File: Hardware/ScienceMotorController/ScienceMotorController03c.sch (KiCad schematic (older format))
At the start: 16 parts

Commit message: changed everything to actuation, added schottky diode, added A/B flags to tiva
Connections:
- net +12V renamed +12VA
- net +3V3 renamed +3.3VA
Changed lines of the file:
@@
 	6950 4250 6950 4150
 Connection ~ 6950 4150
-$Comp
-L power:+12V #PWR?
-U 1 1 5FA7B7CE
-P 7150 4000
-AR Path="/5F7D111E/5FA7B7CE" Ref="#PWR?"  Part="1"
-AR Path="/5F7D111E/5FA660A7/5FA7B7CE" Ref="#PWR?"  Part="1"
-F 0 "#PWR?" H 7150 3850 50  0001 C CNN
-F 1 "+12V" H 7165 4173 50  0000 C CNN
-F 2 "" H 7150 4000 50  0001 C CNN
-F 3 "" H 7150 4000 50  0001 C CNN
-	1    7150 4000
-	1    0    0    -1
-$EndComp
 Wire Wire Line
 	7150 4000 7150 4050
@@
 Wire Wire Line
 	4950 4200 4800 4200
-$Comp
-L power:+3.3V #PWR?
-U 1 1 5FA7B80F
-P 4800 4200
-AR Path="/5F7D111E/5FA7B80F" Ref="#PWR?"  Part="1"
-AR Path="/5F7D111E/5FA660A7/5FA7B80F" Ref="#PWR?"  Part="1"
-F 0 "#PWR?" H 4800 4050 50  0001 C CNN
-F 1 "+3.3V" V 4815 4328 50  0000 L CNN
-F 2 "" H 4800 4200 50  0001 C CNN
-F 3 "" H 4800 4200 50  0001 C CNN
-	1    4800 4200
-	0    -1   -1   0
-$EndComp
-$Comp
-L power:+3.3V #PWR?
-U 1 1 5FA7B815
-P 4800 3900
-AR Path="/5F7D111E/5FA7B815" Ref="#PWR?"  Part="1"
-AR Path="/5F7D111E/5FA660A7/5FA7B815" Ref="#PWR?"  Part="1"
-F 0 "#PWR?" H 4800 3750 50  0001 C CNN
-F 1 "+3.3V" V 4815 4028 50  0000 L CNN
-F 2 "" H 4800 3900 50  0001 C CNN
-F 3 "" H 4800 3900 50  0001 C CNN
-	1    4800 3900
-	0    -1   -1   0
-$EndComp
 Wire Wire Line
 	5300 3900 4800 3900
@@
 Wire Wire Line
 	5300 3800 5150 3800
-$Comp
-L power:+3.3V #PWR?
-U 1 1 5FA7B823
-P 4800 3800
-AR Path="/5F7D111E/5FA7B823" Ref="#PWR?"  Part="1"
-AR Path="/5F7D111E/5FA660A7/5FA7B823" Ref="#PWR?"  Part="1"
-F 0 "#PWR?" H 4800 3650 50  0001 C CNN
-F 1 "+3.3V" V 4815 3928 50  0000 L CNN
-F 2 "" H 4800 3800 50  0001 C CNN
-F 3 "" H 4800 3800 50  0001 C CNN
-	1    4800 3800
-	0    -1   -1   0
-$EndComp
 Wire Wire Line
 	4950 3800 4800 3800
@@
 Text Notes 7100 6950 0    197  ~ 0
 Sheet 03c: Motor Driver 3
+$Comp
+L power:+3.3VA #PWR?
+U 1 1 5F83358B
+P 4800 3800
+F 0 "#PWR?" H 4800 3650 50  0001 C CNN
+F 1 "+3.3VA" V 4815 3927 50  0000 L CNN
+F 2 "" H 4800 3800 50  0001 C CNN
+F 3 "" H 4800 3800 50  0001 C CNN
+	1    4800 3800
+	0    -1   -1   0
+$EndComp
+$Comp
+L power:+3.3VA #PWR?
+U 1 1 5F83453D
+P 4800 3900
+F 0 "#PWR?" H 4800 3750 50  0001 C CNN
+F 1 "+3.3VA" V 4815 4027 50  0000 L CNN
+F 2 "" H 4800 3900 50  0001 C CNN
+F 3 "" H 4800 3900 50  0001 C CNN
+	1    4800 3900
+	0    -1   -1   0
+$EndComp
+$Comp
+L power:+3.3VA #PWR?
+U 1 1 5F83493F
+P 4800 4200
+F 0 "#PWR?" H 4800 4050 50  0001 C CNN
+F 1 "+3.3VA" V 4815 4327 50  0000 L CNN
+F 2 "" H 4800 4200 50  0001 C CNN
+F 3 "" H 4800 4200 50  0001 C CNN
+	1    4800 4200
+	0    -1   -1   0
+$EndComp
+$Comp
+L power:+12VA #PWR?
+U 1 1 5F835353
+P 7150 4000
+F 0 "#PWR?" H 7150 3850 50  0001 C CNN
+F 1 "+12VA" H 7165 4173 50  0000 C CNN
+F 2 "" H 7150 4000 50  0001 C CNN
+F 3 "" H 7150 4000 50  0001 C CNN
+	1    7150 4000
+	1    0    0    -1
+$EndComp
 $EndSCHEMATC

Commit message: fixed hierarchical
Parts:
- added FB? (x2): Ferrite_Bead, symbol Device:Ferrite_Bead_Small
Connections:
- net at U?.1 (OUT_A), U?.25 (OUT_A), U?.30 (OUT_A)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: now also FB?.2; no longer Conn?.2 (V+Log), D?.2 (A)
- net at U?.15 (OUT_B), U?.16 (OUT_B), U?.21 (OUT_B)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: now also FB?.2; no longer Conn?.1 (GND), D?.2 (A)
- net IN_A_3 renamed In_A_3
- net IN_B_3 renamed In_B_3
- new net: Conn?.2 (V+Log), D?.2 (A), FB?.1
- new net: Conn?.1 (GND), D?.2 (A), FB?.1
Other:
- moved on the sheet: Conn?A, Conn?B, D?, R?

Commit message: Fixed 3.3V, added encoders
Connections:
- net +3.3VA: no longer R?.2, U?.6 (CS_DIS)
- new net 3.3VA: R?.2, U?.6 (CS_DIS)
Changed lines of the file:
@@
 $Descr A4 11693 8268
 encoding utf-8
-Sheet 5 10
+Sheet 5 11
 Title ""
 Date ""
@@
 $Comp
 L power:+3.3VA #PWR?
-U 1 1 5F83358B
-P 4800 3800
-AR Path="/5F7D111E/5FA660A7/5F83358B" Ref="#PWR?"  Part="1"
-AR Path="/5F9082FA/5F83358B" Ref="#PWR?"  Part="1"
-AR Path="/5F7148FA/5FA34AD7/5F83358B" Ref="#PWR?"  Part="1"
-F 0 "#PWR?" H 4800 3650 50  0001 C CNN
-F 1 "+3.3VA" V 4815 3927 50  0000 L CNN
-F 2 "" H 4800 3800 50  0001 C CNN
-F 3 "" H 4800 3800 50  0001 C CNN
-	1    4800 3800
-	0    -1   -1   0
-$EndComp
-$Comp
-L power:+3.3VA #PWR?
-U 1 1 5F83453D
-P 4800 3900
-AR Path="/5F7D111E/5FA660A7/5F83453D" Ref="#PWR?"  Part="1"
-AR Path="/5F9082FA/5F83453D" Ref="#PWR?"  Part="1"
-AR Path="/5F7148FA/5FA34AD7/5F83453D" Ref="#PWR?"  Part="1"
-F 0 "#PWR?" H 4800 3750 50  0001 C CNN
-F 1 "+3.3VA" V 4815 4027 50  0000 L CNN
-F 2 "" H 4800 3900 50  0001 C CNN
-F 3 "" H 4800 3900 50  0001 C CNN
-	1    4800 3900
-	0    -1   -1   0
-$EndComp
-$Comp
-L power:+3.3VA #PWR?
 U 1 1 5F83493F
 P 4800 4200
@@
 Text HLabel 3300 4100 0    50   Output ~ 0
 Current_Sense_3
+Text HLabel 4800 3800 0    50   Output ~ 0
+3.3VA
+Text HLabel 4800 3900 0    50   Output ~ 0
+3.3VA
 $EndSCHEMATC

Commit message: added logic line
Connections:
- net 3.3VA is gone; now on net 3.3V: R?.2, U?.6 (CS_DIS)
- net +3.3VA renamed 3.3V
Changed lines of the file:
@@
 Sheet 03c: Motor Driver 3
-$Comp
-L power:+3.3VA #PWR?
-U 1 1 5F83493F
-P 4800 4200
-AR Path="/5F7D111E/5FA660A7/5F83493F" Ref="#PWR?"  Part="1"
-AR Path="/5F9082FA/5F83493F" Ref="#PWR?"  Part="1"
-AR Path="/5F7148FA/5FA34AD7/5F83493F" Ref="#PWR?"  Part="1"
-F 0 "#PWR?" H 4800 4050 50  0001 C CNN
-F 1 "+3.3VA" V 4815 4327 50  0000 L CNN
-F 2 "" H 4800 4200 50  0001 C CNN
-F 3 "" H 4800 4200 50  0001 C CNN
-	1    4800 4200
-	0    -1   -1   0
-$EndComp
 $Comp
 L power:+12VA #PWR?
@@
 Text HLabel 3300 4100 0    50   Output ~ 0
 Current_Sense_3
+Text HLabel 4800 3900 0    50   Output ~ 0
+3.3V
 Text HLabel 4800 3800 0    50   Output ~ 0
-3.3VA
-Text HLabel 4800 3900 0    50   Output ~ 0
-3.3VA
+3.3V
+Text HLabel 4800 4200 0    50   Output ~ 0
+3.3V
 $EndSCHEMATC

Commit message: annotated
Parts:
- C4: renamed from C?; footprint (none) -> Capacitor_SMD:C_0603_1608Metric_Pad1.05x0.95mm_HandSolder
- gave numbers to parts that had none: 16
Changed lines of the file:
@@
 AR Path="/5F7D111E/5FA660A7/5FA7B7BC" Ref="U?"  Part="1"
 AR Path="/5F9082FA/5FA7B7BC" Ref="U?"  Part="1"
-AR Path="/5F7148FA/5FA34AD7/5FA7B7BC" Ref="U?"  Part="1"
-F 0 "U?" H 6100 6137 60  0000 C CNN
+AR Path="/5F7148FA/5FA34AD7/5FA7B7BC" Ref="U4"  Part="1"
+F 0 "U4" H 6100 6137 60  0000 C CNN
 F 1 "VNH5019A_E" H 6100 6031 60  0000 C CNN
 F 2 "" H 5500 5750 60  0001 C CNN
@@
 AR Path="/5F7D111E/5FA660A7/5FA7B7D9" Ref="R?"  Part="1"
 AR Path="/5F9082FA/5FA7B7D9" Ref="R?"  Part="1"
-AR Path="/5F7148FA/5FA34AD7/5FA7B7D9" Ref="R?"  Part="1"
-F 0 "R?" V 5000 3850 50  0000 C CNN
+AR Path="/5F7148FA/5FA34AD7/5FA7B7D9" Ref="R19"  Part="1"
+F 0 "R19" V 5000 3850 50  0000 C CNN
 F 1 "1k" V 5050 4000 50  0000 C CNN
 F 2 "" H 5050 4000 50  0001 C CNN
@@
 AR Path="/5F7D111E/5FA660A7/5FA7B7DF" Ref="R?"  Part="1"
 AR Path="/5F9082FA/5FA7B7DF" Ref="R?"  Part="1"
-AR Path="/5F7148FA/5FA34AD7/5FA7B7DF" Ref="R?"  Part="1"
-F 0 "R?" V 4250 4250 50  0000 C CNN
+AR Path="/5F7148FA/5FA34AD7/5FA7B7DF" Ref="R16"  Part="1"
+F 0 "R16" V 4250 4250 50  0000 C CNN
 F 1 "1k" V 4350 4250 50  0000 C CNN
 F 2 "" H 4350 4250 50  0001 C CNN
@@
 AR Path="/5F7D111E/5FA660A7/5FA7B7E5" Ref="C?"  Part="1"
 AR Path="/5F9082FA/5FA7B7E5" Ref="C?"  Part="1"
-AR Path="/5F7148FA/5FA34AD7/5FA7B7E5" Ref="C?"  Part="1"
-F 0 "C?" H 3658 4204 50  0000 R CNN
+AR Path="/5F7148FA/5FA34AD7/5FA7B7E5" Ref="C4"  Part="1"
+F 0 "C4" H 3658 4204 50  0000 R CNN
 F 1 "33nF" H 3658 4295 50  0000 R CNN
-F 2 "" H 3750 4250 50  0001 C CNN
+F 2 "Capacitor_SMD:C_0603_1608Metric_Pad1.05x0.95mm_HandSolder" H 3750 4250 50  0001 C CNN
 F 3 "~" H 3750 4250 50  0001 C CNN
 	1    3750 4250
@@
 AR Path="/5F7D111E/5FA660A7/5FA7B7EB" Ref="D?"  Part="1"
 AR Path="/5F9082FA/5FA7B7EB" Ref="D?"  Part="1"
-AR Path="/5F7148FA/5FA34AD7/5FA7B7EB" Ref="D?"  Part="1"
-F 0 "D?" V 3550 4100 50  0000 R CNN
+AR Path="/5F7148FA/5FA34AD7/5FA7B7EB" Ref="D10"  Part="1"
+F 0 "D10" V 3550 4100 50  0000 R CNN
 F 1 "D_Zener_Small" V 3450 4150 50  0000 R CNN
 F 2 "" V 3500 4250 50  0001 C CNN
@@
 AR Path="/5F7D111E/5FA660A7/5FA7B7F1" Ref="R?"  Part="1"
 AR Path="/5F9082FA/5FA7B7F1" Ref="R?"  Part="1"
-AR Path="/5F7148FA/5FA34AD7/5FA7B7F1" Ref="R?"  Part="1"
-F 0 "R?" V 3950 4100 50  0000 C CNN
+AR Path="/5F7148FA/5FA34AD7/5FA7B7F1" Ref="R15"  Part="1"
+F 0 "R15" V 3950 4100 50  0000 C CNN
 F 1 "10k" V 4050 4100 50  0000 C CNN
 F 2 "" H 4050 4100 50  0001 C CNN
@@
 AR Path="/5F7D111E/5FA660A7/5FA7B807" Ref="R?"  Part="1"
 AR Path="/5F9082FA/5FA7B807" Ref="R?"  Part="1"
-AR Path="/5F7148FA/5FA34AD7/5FA7B807" Ref="R?"  Part="1"
-F 0 "R?" V 5000 4050 50  0000 C CNN
+AR Path="/5F7148FA/5FA34AD7/5FA7B807" Ref="R20"  Part="1"
+F 0 "R20" V 5000 4050 50  0000 C CNN
 F 1 "1k" V 5050 4200 50  0000 C CNN
 F 2 "" H 5050 4200 50  0001 C CNN
@@
 AR Path="/5F7D111E/5FA660A7/5FA7B81C" Ref="R?"  Part="1"
 AR Path="/5F9082FA/5FA7B81C" Ref="R?"  Part="1"
-AR Path="/5F7148FA/5FA34AD7/5FA7B81C" Ref="R?"  Part="1"
-F 0 "R?" V 5000 3650 50  0000 C CNN
+AR Path="/5F7148FA/5FA34AD7/5FA7B81C" Ref="R18"  Part="1"
+F 0 "R18" V 5000 3650 50  0000 C CNN
 F 1 "1k" V 5050 3800 50  0000 C CNN
 F 2 "" H 5050 3800 50  0001 C CNN
@@
 AR Path="/5F7D111E/5FA660A7/5FA7B82A" Ref="R?"  Part="1"
 AR Path="/5F9082FA/5FA7B82A" Ref="R?"  Part="1"
-AR Path="/5F7148FA/5FA34AD7/5FA7B82A" Ref="R?"  Part="1"
-F 0 "R?" V 5000 3550 50  0000 C CNN
+AR Path="/5F7148FA/5FA34AD7/5FA7B82A" Ref="R17"  Part="1"
+F 0 "R17" V 5000 3550 50  0000 C CNN
 F 1 "1k" V 5050 3700 50  0000 C CNN
 F 2 "" H 5050 3700 50  0001 C CNN
@@
 AR Path="/5F7D111E/5FA660A7/5FA7B834" Ref="R?"  Part="1"
 AR Path="/5F9082FA/5FA7B834" Ref="R?"  Part="1"
-AR Path="/5F7148FA/5FA34AD7/5FA7B834" Ref="R?"  Part="1"
-F 0 "R?" V 5000 4150 50  0000 C CNN
+AR Path="/5F7148FA/5FA34AD7/5FA7B834" Ref="R21"  Part="1"
+F 0 "R21" V 5000 4150 50  0000 C CNN
 F 1 "1k" V 5050 4300 50  0000 C CNN
 F 2 "" H 5050 4300 50  0001 C CNN
@@
 AR Path="/5F7D111E/5FA660A7/5FA7B84C" Ref="#PWR?"  Part="1"
 AR Path="/5F9082FA/5FA7B84C" Ref="#PWR?"  Part="1"
-AR Path="/5F7148FA/5FA34AD7/5FA7B84C" Ref="#PWR?"  Part="1"
-F 0 "#PWR?" H 6450 4500 50  0001 C CNN
+AR Path="/5F7148FA/5FA34AD7/5FA7B84C" Ref="#PWR022"  Part="1"
+F 0 "#PWR022" H 6450 4500 50  0001 C CNN
 F 1 "GND" H 6455 4577 50  0000 C CNN
 F 2 "" H 6450 4750 50  0001 C CNN
@@
 AR Path="/5F7D111E/5FA660A7/5FA7B856" Ref="#PWR?"  Part="1"
 AR Path="/5F9082FA/5FA7B856" Ref="#PWR?"  Part="1"
-AR Path="/5F7148FA/5FA34AD7/5FA7B856" Ref="#PWR?"  Part="1"
-F 0 "#PWR?" H 3750 4250 50  0001 C CNN
+AR Path="/5F7148FA/5FA34AD7/5FA7B856" Ref="#PWR021"  Part="1"
+F 0 "#PWR021" H 3750 4250 50  0001 C CNN
 F 1 "GND" H 3755 4327 50  0000 C CNN
 F 2 "" H 3750 4500 50  0001 C CNN
@@
 AR Path="/5F7D111E/5FA660A7/5FA7B86E" Ref="Conn?"  Part="1"
 AR Path="/5F9082FA/5FA7B86E" Ref="Conn?"  Part="1"
-AR Path="/5F7148FA/5FA34AD7/5FA7B86E" Ref="Conn?"  Part="1"
-F 0 "Conn?" H 8072 3397 60  0000 R CNN
+AR Path="/5F7148FA/5FA34AD7/5FA7B86E" Ref="Conn3"  Part="1"
+F 0 "Conn3" H 8072 3397 60  0000 R CNN
 F 1 "AndersonPP" H 8072 3503 60  0000 R CNN
 F 2 "" H 7950 2800 60  0001 C CNN
@@
 AR Path="/5F7D111E/5FA660A7/5FA7B874" Ref="Conn?"  Part="2"
 AR Path="/5F9082FA/5FA7B874" Ref="Conn?"  Part="2"
-AR Path="/5F7148FA/5FA34AD7/5FA7B874" Ref="Conn?"  Part="2"
-F 0 "Conn?" H 8072 2997 60  0000 R CNN
+AR Path="/5F7148FA/5FA34AD7/5FA7B874" Ref="Conn3"  Part="2"
+F 0 "Conn3" H 8072 2997 60  0000 R CNN
 F 1 "AndersonPP" H 8072 3103 60  0000 R CNN
 F 2 "" H 7950 2400 60  0001 C CNN
@@
 AR Path="/5F7D111E/5FA660A7/5FA7B888" Ref="D?"  Part="1"
 AR Path="/5F9082FA/5FA7B888" Ref="D?"  Part="1"
-AR Path="/5F7148FA/5FA34AD7/5FA7B888" Ref="D?"  Part="1"
-F 0 "D?" H 7950 3200 50  0000 C CNN
+AR Path="/5F7148FA/5FA34AD7/5FA7B888" Ref="D11"  Part="1"
+F 0 "D11" H 7950 3200 50  0000 C CNN
 F 1 "Blue_LED" H 8000 3300 31  0000 C CNN
 F 2 "" V 7850 3250 50  0001 C CNN
@@
 AR Path="/5F7D111E/5FA660A7/5FA7B88E" Ref="D?"  Part="1"
 AR Path="/5F9082FA/5FA7B88E" Ref="D?"  Part="1"
-AR Path="/5F7148FA/5FA34AD7/5FA7B88E" Ref="D?"  Part="1"
-F 0 "D?" H 7950 3600 50  0000 C CNN
+AR Path="/5F7148FA/5FA34AD7/5FA7B88E" Ref="D12"  Part="1"
+F 0 "D12" H 7950 3600 50  0000 C CNN
 F 1 "Blue_LED" H 8000 3700 31  0000 C CNN
 F 2 "" V 7850 3650 50  0001 C CNN
@@
 AR Path="/5F7D111E/5FA660A7/5FA7B894" Ref="R?"  Part="1"
 AR Path="/5F9082FA/5FA7B894" Ref="R?"  Part="1"
-AR Path="/5F7148FA/5FA34AD7/5FA7B894" Ref="R?"  Part="1"
-F 0 "R?" V 8050 3550 50  0000 C CNN
+AR Path="/5F7148FA/5FA34AD7/5FA7B894" Ref="R23"  Part="1"
+F 0 "R23" V 8050 3550 50  0000 C CNN
 F 1 "1.5k" V 8100 3650 39  0000 C CNN
 F 2 "" H 8100 3650 50  0001 C CNN
@@
 AR Path="/5F7D111E/5FA660A7/5FA7B89A" Ref="R?"  Part="1"
 AR Path="/5F9082FA/5FA7B89A" Ref="R?"  Part="1"
-AR Path="/5F7148FA/5FA34AD7/5FA7B89A" Ref="R?"  Part="1"
-F 0 "R?" V 8050 3150 50  0000 C CNN
+AR Path="/5F7148FA/5FA34AD7/5FA7B89A" Ref="R22"  Part="1"
+F 0 "R22" V 8050 3150 50  0000 C CNN
 F 1 "1.5k" V 8100 3250 39  0000 C CNN
 F 2 "" H 8100 3250 50  0001 C CNN
@@
 AR Path="/5F7D111E/5FA660A7/5FA7B8A2" Ref="#PWR?"  Part="1"
 AR Path="/5F9082FA/5FA7B8A2" Ref="#PWR?"  Part="1"
-AR Path="/5F7148FA/5FA34AD7/5FA7B8A2" Ref="#PWR?"  Part="1"
-F 0 "#PWR?" H 8300 3000 50  0001 C CNN
+AR Path="/5F7148FA/5FA34AD7/5FA7B8A2" Ref="#PWR024"  Part="1"
+F 0 "#PWR024" H 8300 3000 50  0001 C CNN
 F 1 "GND" V 8305 3122 50  0000 R CNN
 F 2 "" H 8300 3250 50  0001 C CNN
@@
 AR Path="/5F7D111E/5FA660A7/5FA7B8A8" Ref="#PWR?"  Part="1"
 AR Path="/5F9082FA/5FA7B8A8" Ref="#PWR?"  Part="1"
-AR Path="/5F7148FA/5FA34AD7/5FA7B8A8" Ref="#PWR?"  Part="1"
-F 0 "#PWR?" H 8300 3400 50  0001 C CNN
+AR Path="/5F7148FA/5FA34AD7/5FA7B8A8" Ref="#PWR025"  Part="1"
+F 0 "#PWR025" H 8300 3400 50  0001 C CNN
 F 1 "GND" V 8305 3522 50  0000 R CNN
 F 2 "" H 8300 3650 50  0001 C CNN
@@
 AR Path="/5F7D111E/5FA660A7/5F835353" Ref="#PWR?"  Part="1"
 AR Path="/5F9082FA/5F835353" Ref="#PWR?"  Part="1"
-AR Path="/5F7148FA/5FA34AD7/5F835353" Ref="#PWR?"  Part="1"
-F 0 "#PWR?" H 7150 3850 50  0001 C CNN
+AR Path="/5F7148FA/5FA34AD7/5F835353" Ref="#PWR023"  Part="1"
+F 0 "#PWR023" H 7150 3850 50  0001 C CNN
 F 1 "+12VA" H 7165 4173 50  0000 C CNN
 F 2 "" H 7150 4000 50  0001 C CNN
@@
 P 7300 3050
 AR Path="/5F9082FA/5F9DB37B" Ref="FB?"  Part="1"
-AR Path="/5F7148FA/5FA34AD7/5F9DB37B" Ref="FB?"  Part="1"
-F 0 "FB?" V 7063 3050 50  0000 C CNN
+AR Path="/5F7148FA/5FA34AD7/5F9DB37B" Ref="FB3"  Part="1"
+F 0 "FB3" V 7063 3050 50  0000 C CNN
 F 1 "Ferrite_Bead" V 7154 3050 50  0000 C CNN
 F 2 "" V 7230 3050 50  0001 C CNN
@@
 P 7300 3450
 AR Path="/5F9082FA/5F9DBDAC" Ref="FB?"  Part="1"
-AR Path="/5F7148FA/5FA34AD7/5F9DBDAC" Ref="FB?"  Part="1"
-F 0 "FB?" V 7063 3450 50  0000 C CNN
+AR Path="/5F7148FA/5FA34AD7/5F9DBDAC" Ref="FB4"  Part="1"
+F 0 "FB4" V 7063 3450 50  0000 C CNN
 F 1 "Ferrite_Bead" V 7154 3450 50  0000 C CNN
 F 2 "" V 7230 3450 50  0001 C CNN

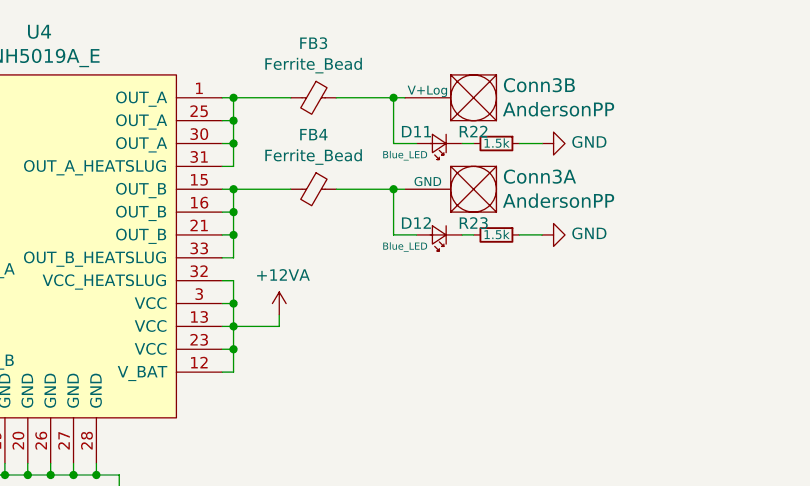
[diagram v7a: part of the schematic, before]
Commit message: assigned most of the footprints
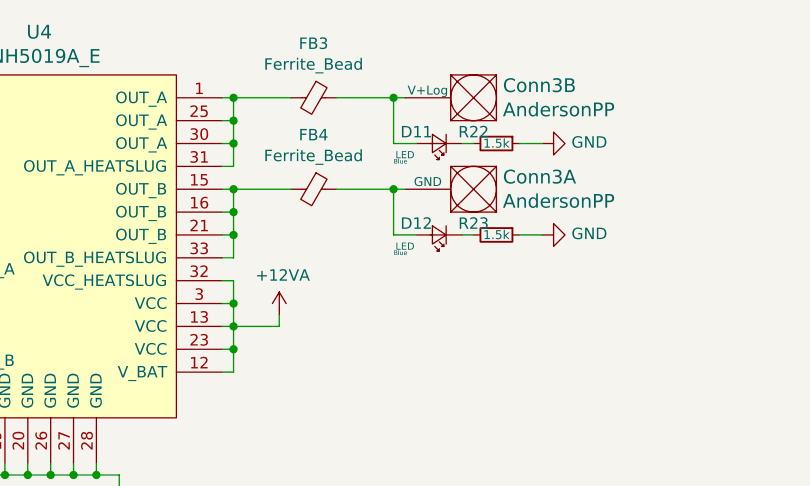
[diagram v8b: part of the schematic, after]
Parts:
- Conn3: footprint (none) -> MRDT_Connectors:Anderson_2_Vertical_Sidy_by_Side
- D10: footprint (none) -> Diode_SMD:D_0603_1608Metric_Pad1.05x0.95mm_HandSolder
- D11, D12: value Blue_LED -> LED; footprint (none) -> LED_SMD:LED_0603_1608Metric_Pad1.05x0.95mm_HandSolder
- R15, R16, R17, R18, R19, R20, R21, R22, R23: footprint (none) -> Resistor_SMD:R_0603_1608Metric_Pad1.05x0.95mm_HandSolder
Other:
- note added: "Blue"
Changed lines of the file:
@@
 F 0 "R19" V 5000 3850 50  0000 C CNN
 F 1 "1k" V 5050 4000 50  0000 C CNN
-F 2 "" H 5050 4000 50  0001 C CNN
+F 2 "Resistor_SMD:R_0603_1608Metric_Pad1.05x0.95mm_HandSolder" H 5050 4000 50  0001 C CNN
 F 3 "~" H 5050 4000 50  0001 C CNN
 	1    5050 4000
@@
 F 0 "R16" V 4250 4250 50  0000 C CNN
 F 1 "1k" V 4350 4250 50  0000 C CNN
-F 2 "" H 4350 4250 50  0001 C CNN
+F 2 "Resistor_SMD:R_0603_1608Metric_Pad1.05x0.95mm_HandSolder" H 4350 4250 50  0001 C CNN
 F 3 "~" H 4350 4250 50  0001 C CNN
 	1    4350 4250
@@
 F 0 "D10" V 3550 4100 50  0000 R CNN
 F 1 "D_Zener_Small" V 3450 4150 50  0000 R CNN
-F 2 "" V 3500 4250 50  0001 C CNN
+F 2 "Diode_SMD:D_0603_1608Metric_Pad1.05x0.95mm_HandSolder" V 3500 4250 50  0001 C CNN
 F 3 "~" V 3500 4250 50  0001 C CNN
 	1    3500 4250
@@
 F 0 "R15" V 3950 4100 50  0000 C CNN
 F 1 "10k" V 4050 4100 50  0000 C CNN
-F 2 "" H 4050 4100 50  0001 C CNN
+F 2 "Resistor_SMD:R_0603_1608Metric_Pad1.05x0.95mm_HandSolder" H 4050 4100 50  0001 C CNN
 F 3 "~" H 4050 4100 50  0001 C CNN
 	1    4050 4100
@@
 F 0 "R20" V 5000 4050 50  0000 C CNN
 F 1 "1k" V 5050 4200 50  0000 C CNN
-F 2 "" H 5050 4200 50  0001 C CNN
+F 2 "Resistor_SMD:R_0603_1608Metric_Pad1.05x0.95mm_HandSolder" H 5050 4200 50  0001 C CNN
 F 3 "~" H 5050 4200 50  0001 C CNN
 	1    5050 4200
@@
 F 0 "R18" V 5000 3650 50  0000 C CNN
 F 1 "1k" V 5050 3800 50  0000 C CNN
-F 2 "" H 5050 3800 50  0001 C CNN
+F 2 "Resistor_SMD:R_0603_1608Metric_Pad1.05x0.95mm_HandSolder" H 5050 3800 50  0001 C CNN
 F 3 "~" H 5050 3800 50  0001 C CNN
 	1    5050 3800
@@
 F 0 "R17" V 5000 3550 50  0000 C CNN
 F 1 "1k" V 5050 3700 50  0000 C CNN
-F 2 "" H 5050 3700 50  0001 C CNN
+F 2 "Resistor_SMD:R_0603_1608Metric_Pad1.05x0.95mm_HandSolder" H 5050 3700 50  0001 C CNN
 F 3 "~" H 5050 3700 50  0001 C CNN
 	1    5050 3700
@@
 F 0 "R21" V 5000 4150 50  0000 C CNN
 F 1 "1k" V 5050 4300 50  0000 C CNN
-F 2 "" H 5050 4300 50  0001 C CNN
+F 2 "Resistor_SMD:R_0603_1608Metric_Pad1.05x0.95mm_HandSolder" H 5050 4300 50  0001 C CNN
 F 3 "~" H 5050 4300 50  0001 C CNN
 	1    5050 4300
@@
 F 0 "Conn3" H 8072 3397 60  0000 R CNN
 F 1 "AndersonPP" H 8072 3503 60  0000 R CNN
-F 2 "" H 7950 2800 60  0001 C CNN
+F 2 "MRDT_Connectors:Anderson_2_Vertical_Sidy_by_Side" H 7950 2800 60  0001 C CNN
 F 3 "" H 7950 2800 60  0001 C CNN
 	1    8100 3350
@@
 F 0 "Conn3" H 8072 2997 60  0000 R CNN
 F 1 "AndersonPP" H 8072 3103 60  0000 R CNN
-F 2 "" H 7950 2400 60  0001 C CNN
+F 2 "MRDT_Connectors:Anderson_2_Vertical_Sidy_by_Side" H 7950 2400 60  0001 C CNN
 F 3 "" H 7950 2400 60  0001 C CNN
 	2    8100 2950
@@
 AR Path="/5F7148FA/5FA34AD7/5FA7B888" Ref="D11"  Part="1"
 F 0 "D11" H 7950 3200 50  0000 C CNN
-F 1 "Blue_LED" H 8000 3300 31  0000 C CNN
-F 2 "" V 7850 3250 50  0001 C CNN
+F 1 "LED" H 8000 3300 31  0000 C CNN
+F 2 "LED_SMD:LED_0603_1608Metric_Pad1.05x0.95mm_HandSolder" V 7850 3250 50  0001 C CNN
 F 3 "~" V 7850 3250 50  0001 C CNN
 	1    7850 3250
@@
 AR Path="/5F7148FA/5FA34AD7/5FA7B88E" Ref="D12"  Part="1"
 F 0 "D12" H 7950 3600 50  0000 C CNN
-F 1 "Blue_LED" H 8000 3700 31  0000 C CNN
-F 2 "" V 7850 3650 50  0001 C CNN
+F 1 "LED" H 8000 3700 31  0000 C CNN
+F 2 "LED_SMD:LED_0603_1608Metric_Pad1.05x0.95mm_HandSolder" V 7850 3650 50  0001 C CNN
 F 3 "~" V 7850 3650 50  0001 C CNN
 	1    7850 3650
@@
 F 0 "R23" V 8050 3550 50  0000 C CNN
 F 1 "1.5k" V 8100 3650 39  0000 C CNN
-F 2 "" H 8100 3650 50  0001 C CNN
+F 2 "Resistor_SMD:R_0603_1608Metric_Pad1.05x0.95mm_HandSolder" H 8100 3650 50  0001 C CNN
 F 3 "~" H 8100 3650 50  0001 C CNN
 	1    8100 3650
@@
 F 0 "R22" V 8050 3150 50  0000 C CNN
 F 1 "1.5k" V 8100 3250 39  0000 C CNN
-F 2 "" H 8100 3250 50  0001 C CNN
+F 2 "Resistor_SMD:R_0603_1608Metric_Pad1.05x0.95mm_HandSolder" H 8100 3250 50  0001 C CNN
 F 3 "~" H 8100 3250 50  0001 C CNN
 	1    8100 3250
@@
 Text HLabel 4800 4200 0    50   Output ~ 0
 3.3V
+Text Notes 7650 3350 0    20   ~ 0
+Blue
+Text Notes 7650 3750 0    20   ~ 0
+Blue
 $EndSCHEMATC
